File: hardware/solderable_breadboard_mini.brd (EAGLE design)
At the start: 47 x 34.3 mm, 37 parts

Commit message: Adding some flame logos to the board.
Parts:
- added LOGO3, LOGO4: SFE_LOGO_FLAME.1_INCH, SparkFun-Aesthetics:SFE_LOGO_FLAME_.1
- moved LOGO2 2.00 mm to (14.1, 16.9)
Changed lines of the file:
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@@
 <setting verticaltext="up"/>
 </settings>
-<grid distance="0.05" unitdist="inch" unit="inch" style="lines" multiple="1" display="yes" altdistance="0.005" altunitdist="inch" altunit="inch"/>
+<grid distance="1" unitdist="mm" unit="mm" style="lines" multiple="1" display="yes" altdistance="0.1" altunitdist="mm" altunit="mm"/>
 <layers>
 <layer number="1" name="Top" color="4" fill="1" visible="yes" active="yes"/>
@@
 <layer number="49" name="Reference" color="7" fill="1" visible="yes" active="yes"/>
 <layer number="50" name="dxf" color="7" fill="1" visible="no" active="no"/>
-<layer number="51" name="tDocu" color="6" fill="1" visible="yes" active="yes"/>
+<layer number="51" name="tDocu" color="6" fill="1" visible="no" active="yes"/>
 <layer number="52" name="bDocu" color="7" fill="1" visible="no" active="yes"/>
 <layer number="53" name="tGND_GNDA" color="7" fill="9" visible="no" active="no"/>
@@
 <dimension x1="5" y1="35" x2="42" y2="35" x3="23.5" y3="36" textsize="1.778" textratio="15" layer="51" visible="yes"/>
 <dimension x1="5" y1="35" x2="42" y2="35" x3="23.5" y3="39" textsize="1.778" textratio="15" layer="51" unit="inch" precision="3" visible="yes"/>
-<text x="9.525" y="16.51" size="1.27" layer="21" font="vector" ratio="15">Solderable Breadboard Mini</text>
+<text x="10.525" y="16.51" size="1.27" layer="21" font="vector" ratio="15">Solderable Breadboard Mini</text>
 </plain>
 <attributes>
@@
 <element name="JP34" library="SparkFun-Connectors" package="1X05_NO_SILK" value=" " x="43.815" y="20.955" rot="R90"/>
 <element name="LOGO1" library="SparkFun-Aesthetics" package="SFE_LOGO_NAME_.1" value="SFE_LOGO_NAME.1_INCH" x="29.21" y="15.24" rot="MR0"/>
-<element name="LOGO2" library="SparkFun-Aesthetics" package="OSHW-LOGO-M" value="OSHW-LOGOM" x="12.065" y="16.891" rot="MR0"/>
+<element name="LOGO2" library="SparkFun-Aesthetics" package="OSHW-LOGO-M" value="OSHW-LOGOM" x="14.065" y="16.891" rot="MR0"/>
+<element name="LOGO3" library="SparkFun-Aesthetics" package="SFE_LOGO_FLAME_.1" value="SFE_LOGO_FLAME.1_INCH" x="8" y="15.9"/>
+<element name="LOGO4" library="SparkFun-Aesthetics" package="SFE_LOGO_FLAME_.1" value="SFE_LOGO_FLAME.1_INCH" x="34" y="16" rot="MR0"/>
 </elements>
 <signals>

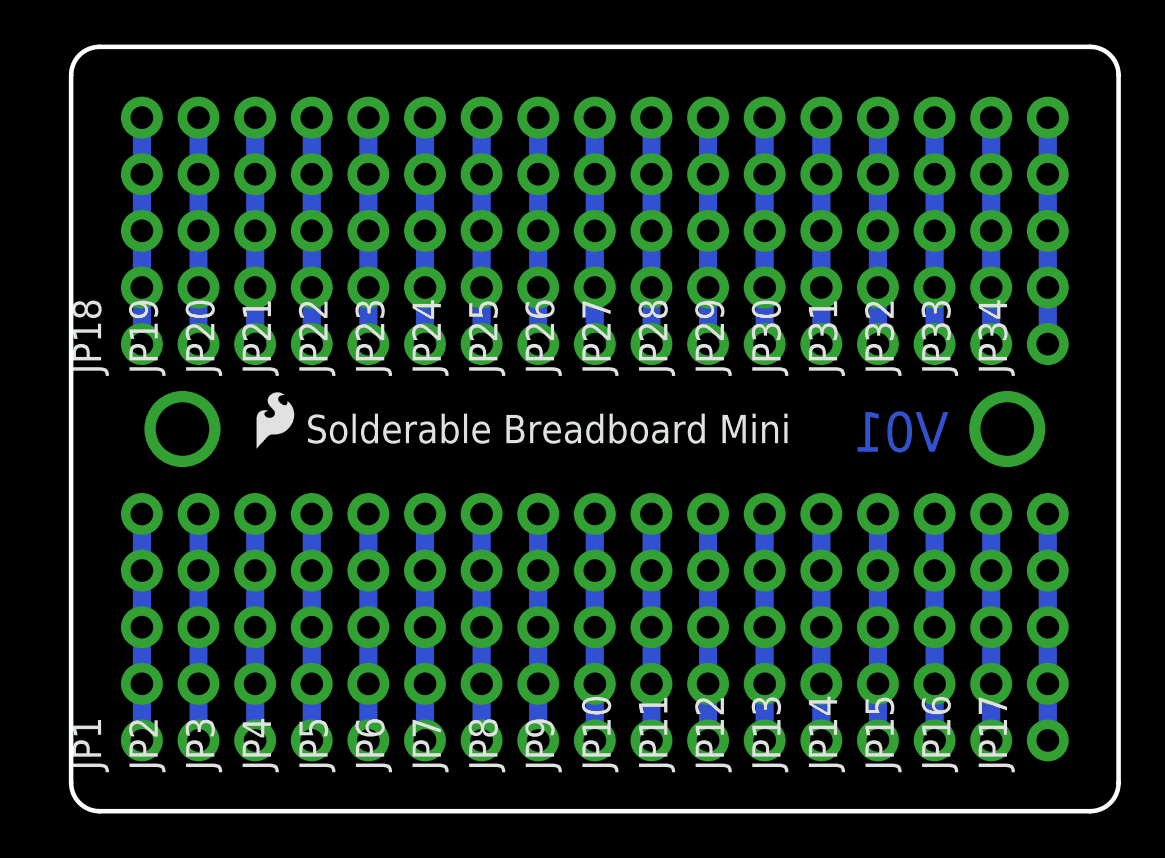
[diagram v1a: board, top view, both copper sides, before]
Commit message: Ready for reds
Outline a tiny bit smaller.
Silkscreen elements more balanced.
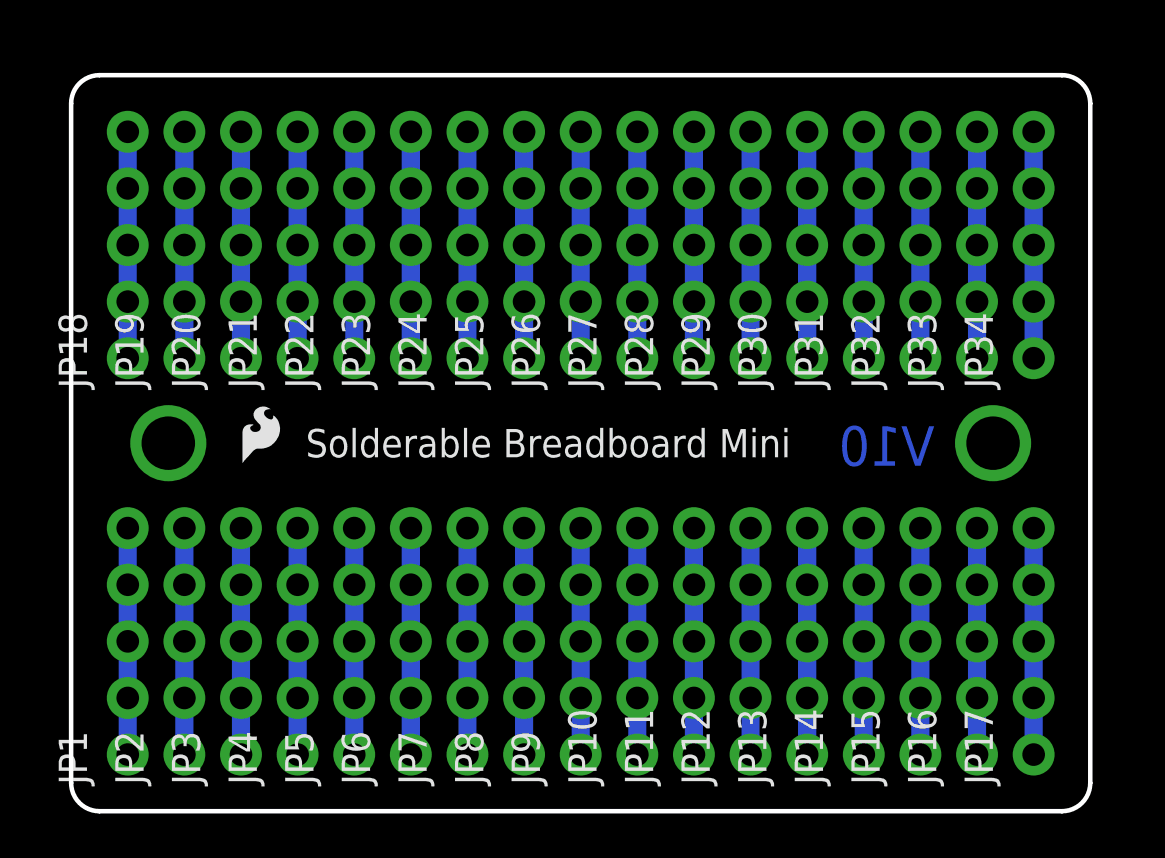
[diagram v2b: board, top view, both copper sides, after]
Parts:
- moved LOGO4 2.62 mm to (31.5, 15.4)
- moved JP10 0.90 mm to (25.4, 2.54)
- moved JP5 0.90 mm to (12.7, 2.54)
- moved JP9 0.90 mm to (22.9, 2.54)
- moved LOGO1 0.90 mm to (28.6, 14.6)
- moved JP3 0.90 mm to (7.62, 2.54)
- moved JP1 0.90 mm to (2.54, 2.54)
- moved JP2 0.90 mm to (5.08, 2.54)
- moved JP22 0.90 mm to (12.7, 20.3)
- moved JP26 0.90 mm to (22.9, 20.3)
- moved JP27 0.90 mm to (25.4, 20.3)
- moved JP4 0.90 mm to (10.2, 2.54)
- moved JP6 0.90 mm to (15.2, 2.54)
- moved LOGO3 0.90 mm to (7.37, 15.3)
- moved JP20 0.90 mm to (7.62, 20.3)
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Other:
- board size 47 x 34.3 mm -> 45.7 x 33 mm
- board text added: "V10"
- board text removed: "V01"
